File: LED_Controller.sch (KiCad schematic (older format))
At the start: 26 parts, among them CON1 CONNECTOR, CON2 CONNECTOR, CON3 CONNECTOR, CON4 CONNECTOR, CON5 PWR_CON, CON6 AVR-ISP-10, CON7 AVR-ISP-6, IC1 ATMEGA328P-P, Q1 STS8DN3LLH5, Q2 STS8DN3LLH5, Q3 STS8DN3LLH5

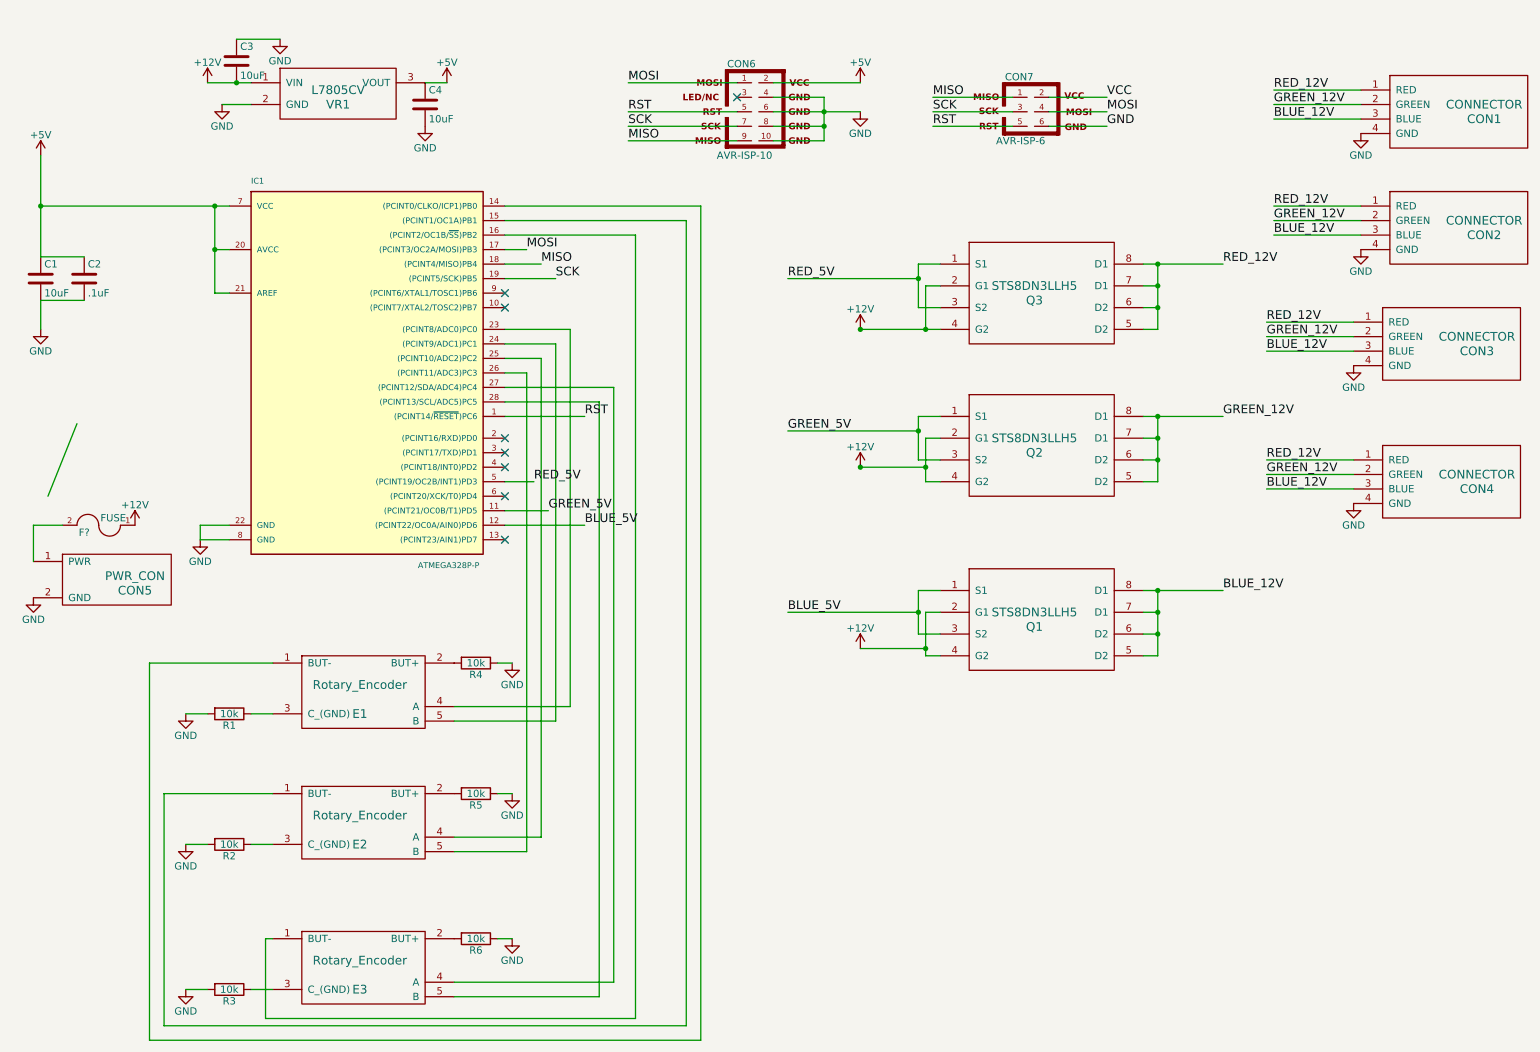
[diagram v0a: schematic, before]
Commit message: Minor Changes
Added a pull-up resistor to RST, to ensure chip is not reset during
normal use. Some minor changes to the track layout.
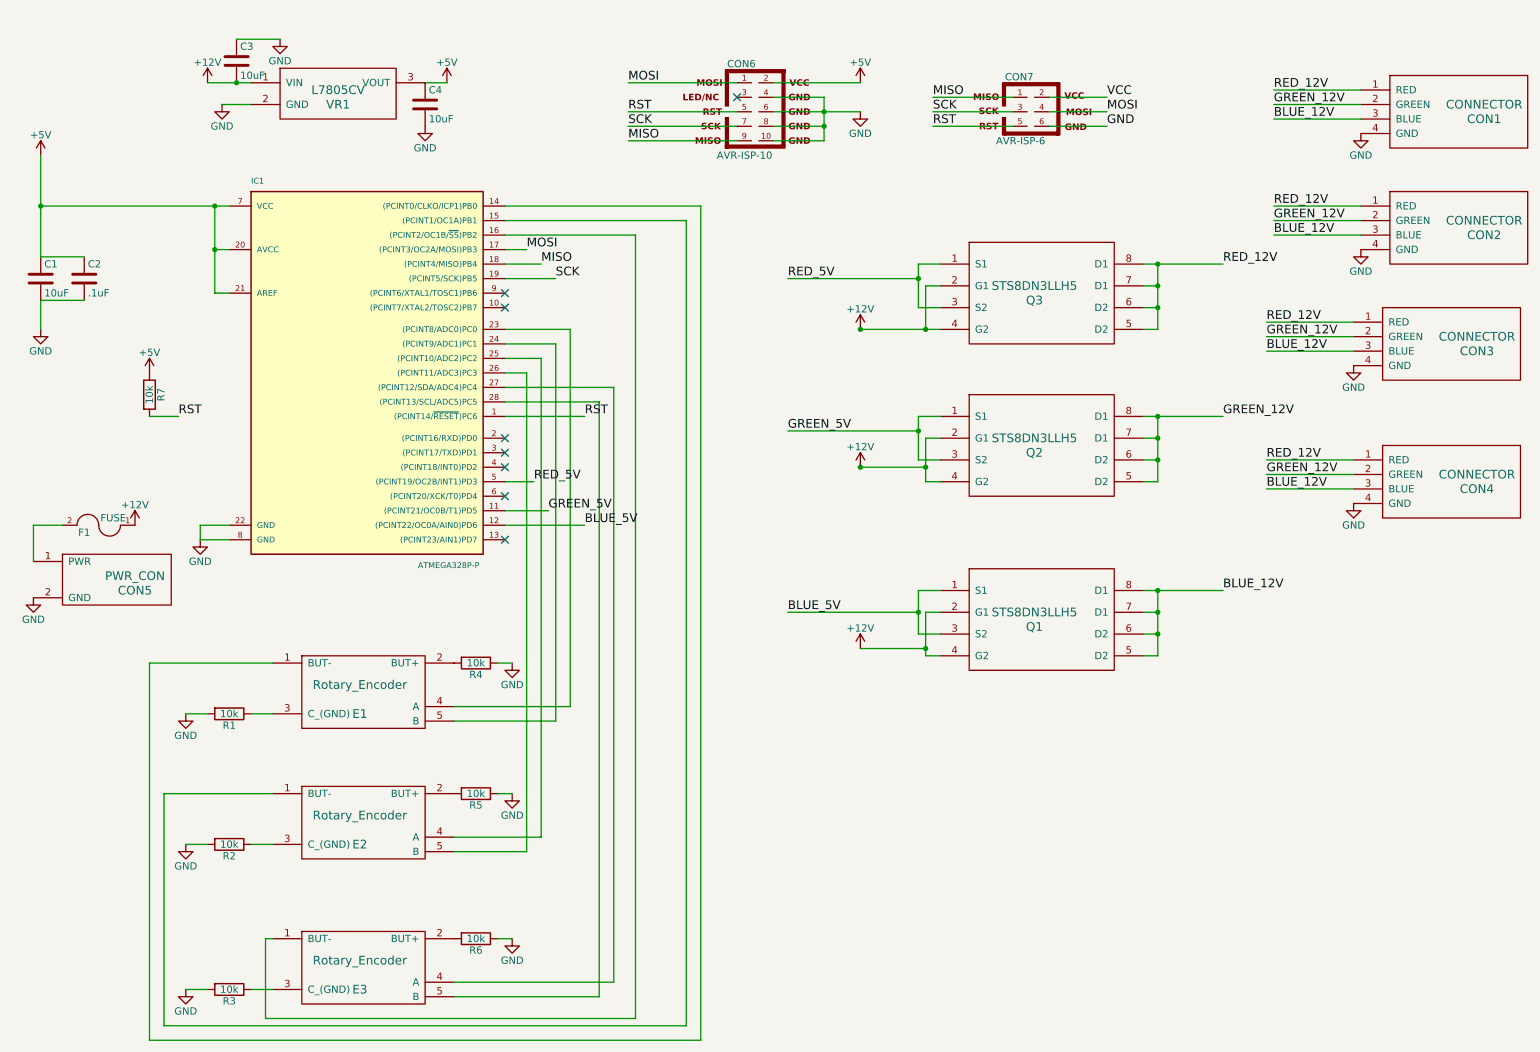
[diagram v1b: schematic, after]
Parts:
- added R7: 10k, LEDs:LED_0603, symbol R
- gave numbers to parts that had none: 1
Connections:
- net +5V: now also R7.1
- net RST: now also R7.2
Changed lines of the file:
@@
 $EndComp
 $Comp
-L GND #PWR022
+L GND #PWR021
 U 1 1 56B80FD6
 P 9850 2150
-F 0 "#PWR022" H 9850 1900 50  0001 C CNN
+F 0 "#PWR021" H 9850 1900 50  0001 C CNN
 F 1 "GND" H 9850 2000 50  0000 C CNN
 F 2 "" H 9850 2150 60  0000 C CNN
@@
 $EndComp
 $Comp
-L GND #PWR023
+L GND #PWR022
 U 1 1 56B8118A
 P 9800 2950
-F 0 "#PWR023" H 9800 2700 50  0001 C CNN
+F 0 "#PWR022" H 9800 2700 50  0001 C CNN
 F 1 "GND" H 9800 2800 50  0000 C CNN
 F 2 "" H 9800 2950 60  0000 C CNN
@@
 	1950 2450 2050 2450
 Wire Wire Line
-	1950 1850 1950 2150
-Wire Wire Line
-	1950 2150 1950 2450
-Wire Wire Line
-	750  1500 750  1850
-Wire Wire Line
-	750  1850 750  2200
+	1950 1850 1950 2450
+Wire Wire Line
+	750  1500 750  2200
 Wire Wire Line
 	6850 2700 6850 2400
@@
 	6850 3750 6950 3750
 Wire Wire Line
-	6850 3450 6850 3650
-Wire Wire Line
-	6850 3650 6850 3750
+	6850 3450 6850 3750
 Wire Wire Line
 	6950 3450 6850 3450
@@
 	6850 4950 6950 4950
 Wire Wire Line
-	6850 4650 6850 4900
-Wire Wire Line
-	6850 4900 6850 4950
+	6850 4650 6850 4950
 Wire Wire Line
 	6950 4650 6850 4650
@@
 	6800 4800 6950 4800
 Wire Wire Line
-	6800 4500 6800 4650
-Wire Wire Line
-	6800 4650 6800 4800
+	6800 4500 6800 4800
 Wire Wire Line
 	6950 4500 6800 4500
@@
 	6800 3600 6950 3600
 Wire Wire Line
-	6800 3300 6800 3400
-Wire Wire Line
-	6800 3400 6800 3600
+	6800 3300 6800 3600
 Wire Wire Line
 	6950 3300 6800 3300
@@
 	6800 2550 6950 2550
 Wire Wire Line
-	6800 2250 6800 2350
-Wire Wire Line
-	6800 2350 6800 2550
+	6800 2250 6800 2550
 Wire Wire Line
 	6950 2250 6800 2250
@@
 	8450 4950 8350 4950
 Wire Wire Line
-	8450 4500 8450 4650
-Wire Wire Line
-	8450 4650 8450 4800
-Wire Wire Line
-	8450 4800 8450 4950
+	8450 4500 8450 4950
 Connection ~ 8450 2400
 Wire Wire Line
@@
 	8450 2550 8350 2550
 Wire Wire Line
-	8450 2250 8450 2400
-Wire Wire Line
-	8450 2400 8450 2550
-Wire Wire Line
-	8450 2550 8450 2700
+	8450 2250 8450 2700
 Connection ~ 8450 3450
 Wire Wire Line
@@
 	8450 3750 8350 3750
 Wire Wire Line
-	8450 3300 8450 3450
-Wire Wire Line
-	8450 3450 8450 3600
-Wire Wire Line
-	8450 3600 8450 3750
+	8450 3300 8450 3750
 Wire Wire Line
 	1900 7250 1750 7250
@@
 	5800 1100 6150 1100
 Wire Wire Line
-	6150 1100 6150 1200
-Wire Wire Line
-	6150 1200 6150 1300
-Wire Wire Line
-	6150 1300 6150 1400
-Wire Wire Line
-	5800 1200 6150 1200
-Wire Wire Line
-	6150 1200 6400 1200
+	6150 1100 6150 1400
+Wire Wire Line
+	5800 1200 6400 1200
 Connection ~ 6150 1200
 Wire Wire Line
@@
 	2050 4050 1850 4050
 Wire Wire Line
-	750  1850 1950 1850
-Wire Wire Line
-	1950 1850 2050 1850
+	750  1850 2050 1850
 Wire Wire Line
 	8450 4800 8350 4800
@@
 	9800 3800 9200 3800
 Wire Wire Line
-	8350 2250 8450 2250
-Wire Wire Line
-	8450 2250 8900 2250
-Wire Wire Line
-	8350 3300 8450 3300
-Wire Wire Line
-	8450 3300 8900 3300
-Wire Wire Line
-	8350 4500 8450 4500
-Wire Wire Line
-	8450 4500 8900 4500
+	8350 2250 8900 2250
+Wire Wire Line
+	8350 3300 8900 3300
+Wire Wire Line
+	8350 4500 8900 4500
 Wire Wire Line
 	1850 4050 1850 4150
@@
 	2400 700  2100 700
 Wire Wire Line
-	1900 1000 2100 1000
-Wire Wire Line
-	2100 1000 2200 1000
+	1900 1000 2200 1000
 Connection ~ 2100 1000
 $Comp
-L +12V #PWR024
+L +12V #PWR023
 U 1 1 56BAC237
 P 1900 1000
-F 0 "#PWR024" H 1900 850 50  0001 C CNN
+F 0 "#PWR023" H 1900 850 50  0001 C CNN
 F 1 "+12V" H 1900 1140 50  0000 C CNN
 F 2 "" H 1900 1000 60  0000 C CNN
@@
 $EndComp
 $Comp
-L +12V #PWR025
+L +12V #PWR024
 U 1 1 56BAC558
 P 6400 2700
-F 0 "#PWR025" H 6400 2550 50  0001 C CNN
+F 0 "#PWR024" H 6400 2550 50  0001 C CNN
 F 1 "+12V" H 6400 2840 50  0000 C CNN
 F 2 "" H 6400 2700 60  0000 C CNN
@@
 $EndComp
 Wire Wire Line
-	6400 2700 6850 2700
-Wire Wire Line
-	6850 2700 6950 2700
-$Comp
-L FUSE F?
+	6400 2700 6950 2700
+$Comp
+L FUSE F1
 U 1 1 56BE5862
 P 1150 4050
-F 0 "F?" H 1250 4100 50  0000 C CNN
+F 0 "F1" H 1250 4100 50  0000 C CNN
 F 1 "FUSE" H 1050 4000 50  0000 C CNN
-F 2 "" H 1150 4050 60  0000 C CNN
+F 2 "" H 1150 4050 60  0001 C CNN
 F 3 "" H 1150 4050 60  0000 C CNN
 	1    1150 4050
@@
 $EndComp
 Wire Wire Line
-	800  3850 1000 3350
-Wire Wire Line
 	700  4300 700  4050
 Wire Wire Line
 	700  4050 900  4050
 $Comp
-L +12V #PWR?
+L +12V #PWR025
 U 1 1 56BE5D46
 P 1400 4050
-F 0 "#PWR?" H 1400 3900 50  0001 C CNN
+F 0 "#PWR025" H 1400 3900 50  0001 C CNN
 F 1 "+12V" H 1400 4190 50  0000 C CNN
 F 2 "" H 1400 4050 60  0000 C CNN
@@
 	1    0    0    -1
 $EndComp
+$Comp
+L +5V #PWR026
+U 1 1 56C11944
+P 1500 3000
+F 0 "#PWR026" H 1500 2850 50  0001 C CNN
+F 1 "+5V" H 1500 3140 50  0000 C CNN
+F 2 "" H 1500 3000 60  0000 C CNN
+F 3 "" H 1500 3000 60  0000 C CNN
+	1    1500 3000
+	1    0    0    -1
+$EndComp
+$Comp
+L R R7
+U 1 1 56C11A0E
+P 1500 3150
+F 0 "R7" V 1580 3150 50  0000 C CNN
+F 1 "10k" V 1500 3150 50  0000 C CNN
+F 2 "LEDs:LED_0603" V 1430 3150 30  0001 C CNN
+F 3 "" H 1500 3150 30  0000 C CNN
+	1    1500 3150
+	1    0    0    -1
+$EndComp
+Text Label 1700 3300 0    60   ~ 0
+RST
+Wire Wire Line
+	1500 3300 1700 3300
 $EndSCHEMATC
